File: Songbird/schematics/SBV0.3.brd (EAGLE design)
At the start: 53.3 x 73.6 mm, 50 parts, among them IC1 TLC2272344P, J1 AVR_SPI_PRG_6NS, U1 USD-SOCKETNEW, U2 ARDUINO_R3_SHIELDNOLABELS, U5 TLC2272344P

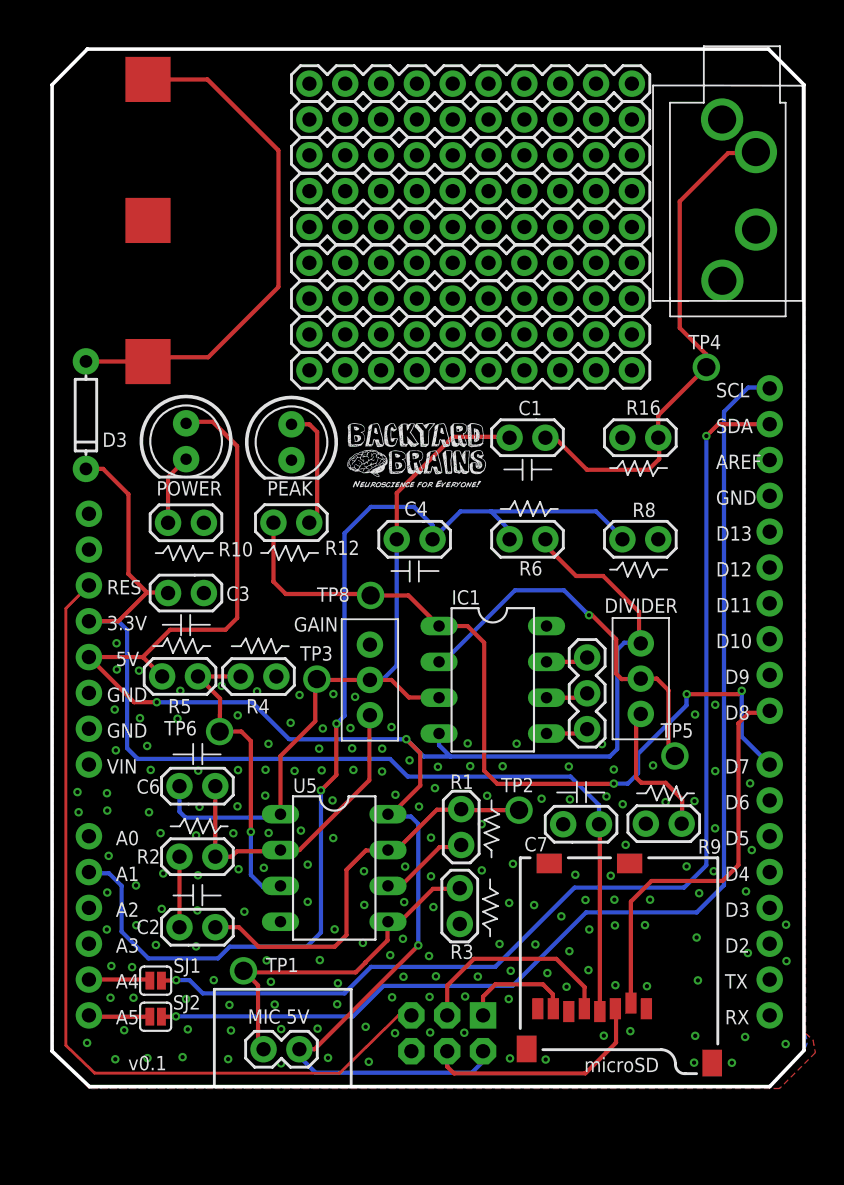
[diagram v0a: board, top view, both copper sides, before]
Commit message: Deleted uncessacary files, various updates / tweaks to model test utility
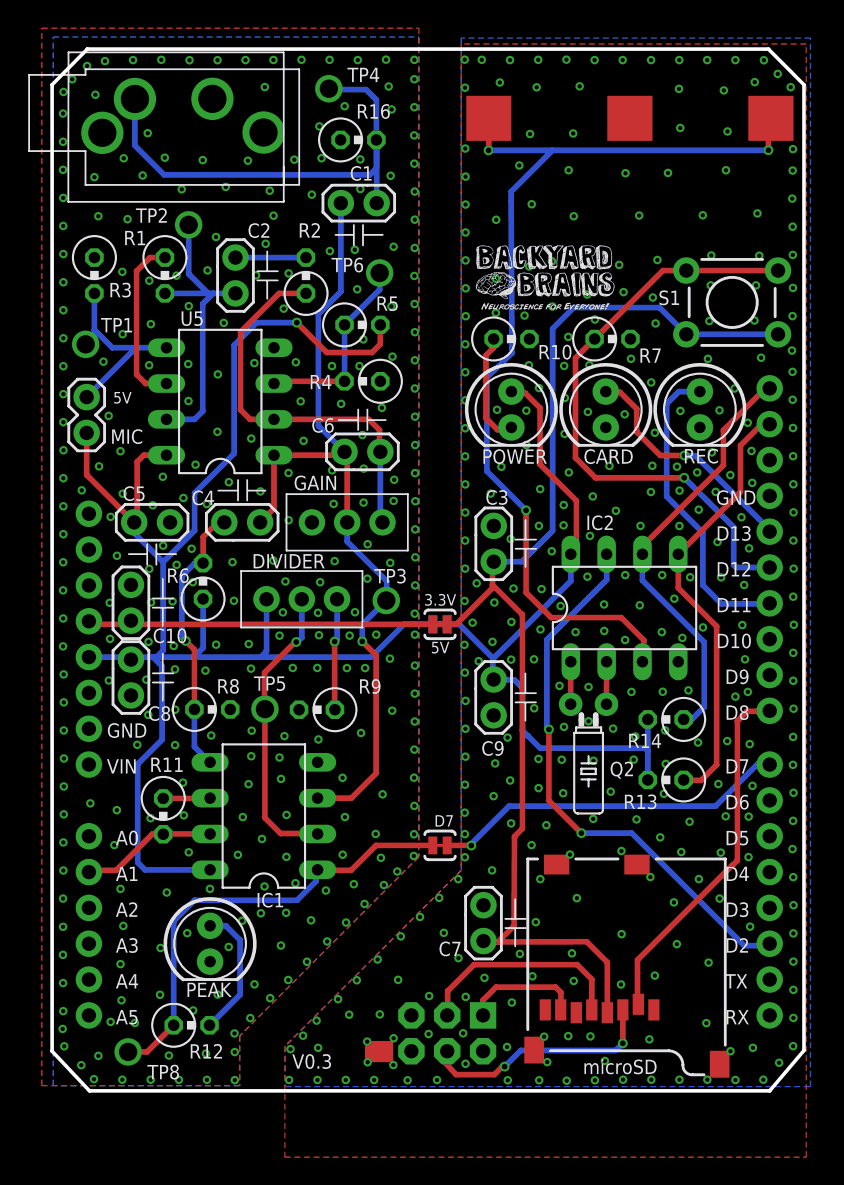
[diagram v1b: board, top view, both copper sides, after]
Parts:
- removed BATT: BATTERY-16MMSMD, byb:16M_BATT_SMD
- removed D3: (no value), SparkFun-DiscreteSemi:DIODE-1N4148
- removed J10, J11, J12, J4, J5, J6, J7, J8, J9: (no value), SparkFun-Connectors:1X10
- removed J14: (no value), SparkFun-Connectors:1X03
- removed SJ1, SJ2: SOLDERJUMPERNC, SparkFun-Passives:SJ_2S
- added 3.3V, 5V, D7: SOLDERJUMPERTRACE, SparkFun:SJ_2S-TRACE
- added BATT1: BATTERY-16MMSMD, byb:16M_BATT_SMD
- added C10, C5, C8, C9: 10uf, 1MaxBYB:M2-CAP
- added CARD, REC: (no value), SparkFun-LED:LED5MM
- added IC2: DS1307, 1MaxBYB:DIL08
- added JP2: M01SMD-4.5X1.5, 1MaxBYB:PAD-1.5X4.5
- added Q2: 32.768kHz, 1MaxBYB:TC26H
- added R11: 300, resistor:0309V
- added R13, R14: 4.7k, resistor:0309V
- added R7: 10k, resistor:0309V
- added S1: (no value), 1MaxBYB:TACTILE-PTH
- R1, R10, R12, R16, R2, R3, R4, R5, R6, R8, R9: device 1MaxBYB:M2-RES -> resistor:0309V
- moved R3 51.7 mm to (3.00, 57.5), turned to 270 degrees
- moved J2 47.9 mm to (2.45, 48.9), turned to 270 degrees
- moved TP2 47.6 mm to (9.68, 61.1)
- moved C2 46.3 mm to (13.0, 57.5), turned to 90 degrees
- moved TP1 45.8 mm to (2.38, 52.6)
- moved R1 44.4 mm to (8.00, 57.5), turned to 270 degrees
- moved R2 41.9 mm to (18.0, 57.5), turned to 90 degrees
- moved J3 41.2 mm to (7.72, 68.8), turned to 0 degrees
- moved TP8 36.6 mm to (5.39, 2.46)
- moved R12 36.3 mm to (9.89, 4.35)
- moved PEAK 36.0 mm to (11.2, 10.1)
- moved TP6 34.4 mm to (23.2, 57.7), turned to 180 degrees
- moved U5 34.0 mm to (11.9, 48.6), turned to 90 degrees
- moved TP4 33.3 mm to (19.6, 70.7)
- moved R8 32.6 mm to (11.4, 26.7)
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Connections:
- removed net D2: U2.D2
- new net ASD: D7.1, IC1.1, R12.1, TP8.P$1
- new net GND-D: BATT1.NEG, C3.2, C7.2, C9.1, CARD.K, IC2.4, JP2.P$1, R10.2, R7.2, REC.K, U1.6, U1.CD1, U1.CD2, U1.GND1, U1.GND3, U2.GND@2
- new net N$13: CARD.A, U2.D13
- new net N$15: BATT1.POS1, BATT1.POS2, IC2.3
- new net PREA1: C4.2, IC1.5, R6.2, R8.1
- new net SQW: IC2.7, U2.D2
- net 3.3V: now also 3.3V.1, 3.3V.2, C10.1, S1.3, S1.4; no longer D3.C
- net 5V: now also 5V.1, 5V.2, C5.1, C8.2, C9.2, DIVIDER.1, IC1.8, IC2.8, R13.2, R14.2; no longer IC1.4, J1.2
- net A1: now also IC1.7, R11.2; no longer C4.2, R6.2, R8.1
- net A4: no longer SJ1.2
- net A5: no longer SJ2.2
- net D7: now also D7.2; no longer IC1.1, R12.1, TP8.P$1
- net GND: now also C10.2, C5.2, C8.1, IC1.4; no longer BATT.NEG, C3.2, C7.2, IC1.8, J1.6, R10.2, U1.6, U1.CD1, U1.CD2, U1.GND1, U1.GND3, U2.GND@2
- net N$10: now also IC2.2, Q2.1; no longer IC1.7, J14.1
- net N$12: now also R7.1, S1.1, S1.2, U2.D12; no longer DIVIDER.1
- net N$2: now also REC.A, U2.D11; no longer BATT.POS1, BATT.POS2, D3.A
- net N$8: now also IC2.1, Q2.2; no longer IC1.5, J14.3
- net N$9: now also R11.1; no longer J14.2
- net RES: no longer J1.5
- net SCL: now also IC2.6, R14.1; no longer SJ2.1
- net SDA: now also IC2.5, R13.1; no longer SJ1.1
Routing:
- net N$15: track 0.00 -> 70.2 mm, vias 0 -> 3
- net A1: track 76.9 -> 9.74 mm, vias 2 -> 0
- net RES: track 60.2 -> 0.00 mm
- net SCL: track 81.3 -> 30.1 mm, vias 1 -> 0
- net SDA: track 78.1 -> 31.1 mm, vias 2 -> 0
- net N$12: track 0.00 -> 42.6 mm, vias 0 -> 1
- net SQW: track 0.00 -> 39.3 mm, vias 0 -> 2
- net D7: track 58.7 -> 25.3 mm, vias 3 -> 1
- net ASD: track 0.00 -> 32.4 mm
- net 3.3V: track 78.9 -> 108.8 mm
- net 5V: track 137.1 -> 162.0 mm, vias 3 -> 1
- net PREA1: track 0.00 -> 19.9 mm, vias 0 -> 1
- net N$13: track 0.00 -> 16.8 mm, vias 0 -> 1
- net N$2: track 36.8 -> 21.9 mm
- net N$1: track 24.9 -> 14.5 mm
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- added copper zone on layer 1, net GND-D
- added copper zone on layer 16, net GND-D
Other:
- board size 53.3 x 73.6 mm -> 53.3 x 73.9 mm
- board text added: "MIC"
- board text added: "V0.3"
- board text removed: "3.3V"
- board text removed: "AREF"
- board text removed: "MIC 5V"
- board text removed: "RES"
- board text removed: "SCL"
- board text removed: "SDA"
- board text removed: "v0.1"
